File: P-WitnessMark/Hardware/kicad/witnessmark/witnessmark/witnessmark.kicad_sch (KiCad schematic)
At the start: 46 parts, among them J2 Conn_01x04, J3 Conn_01x11, J4 Conn_01x05, J5 USB_C_Receptacle_USB2.0_16P, U1 STM32U585RITx, U2 AP2112K-3.3, U3 SLS32AIA010MHUSON10XTMA2, U4 USBLC6-2SC6, Y1 Crystal

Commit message: WitnessMark: fix VDDA cap shorting GND to +3V3 (rail merge); GND now distinct
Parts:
- removed C8: 100nF, Capacitor_SMD:C_0603_1608Metric, symbol Device:C
- removed C9: 4.7µF, Capacitor_SMD:C_0603_1608Metric, symbol Device:C
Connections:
- net +3V3: no longer C1.2, C10.2, C11.2, C12.2, C13.1, C14.2, C15.2, C2.2, C3.2, C4.1, C5.1, C6.1, C7.1, J2.4 (Pin_4), J3.3 (Pin_3), J4.3 (Pin_3), J5.A1 (GND), J5.A12 (GND), J5.B1 (GND), J5.B12 (GND), J5.SH (SHIELD), R1.2, R4.1, R5.1, R6.2, S1.1, S1.2, U1.12 (VSSA), U1.18 (VSS), U1.31 (VSS), U1.47 (VSS), U1.63 (VSS), U2.2 (GND), U3.1 (GND), U3.11 (EP), U4.2 (GND)
- new net GND: C1.2, C10.2, C11.2, C12.2, C13.1, C14.2, C15.2, C2.2, C3.2, C4.1, C5.1, C6.1, C7.1, J2.4 (Pin_4), J3.3 (Pin_3), J4.3 (Pin_3), J5.A1 (GND), J5.A12 (GND), J5.B1 (GND), J5.B12 (GND), J5.SH (SHIELD), R1.2, R4.1, R5.1, R6.2, S1.1, S1.2, U1.12 (VSSA), U1.18 (VSS), U1.31 (VSS), U1.47 (VSS), U1.63 (VSS), U2.2 (GND), U3.1 (GND), U3.11 (EP), U4.2 (GND)
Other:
- moved on the sheet: J5, R4, R5

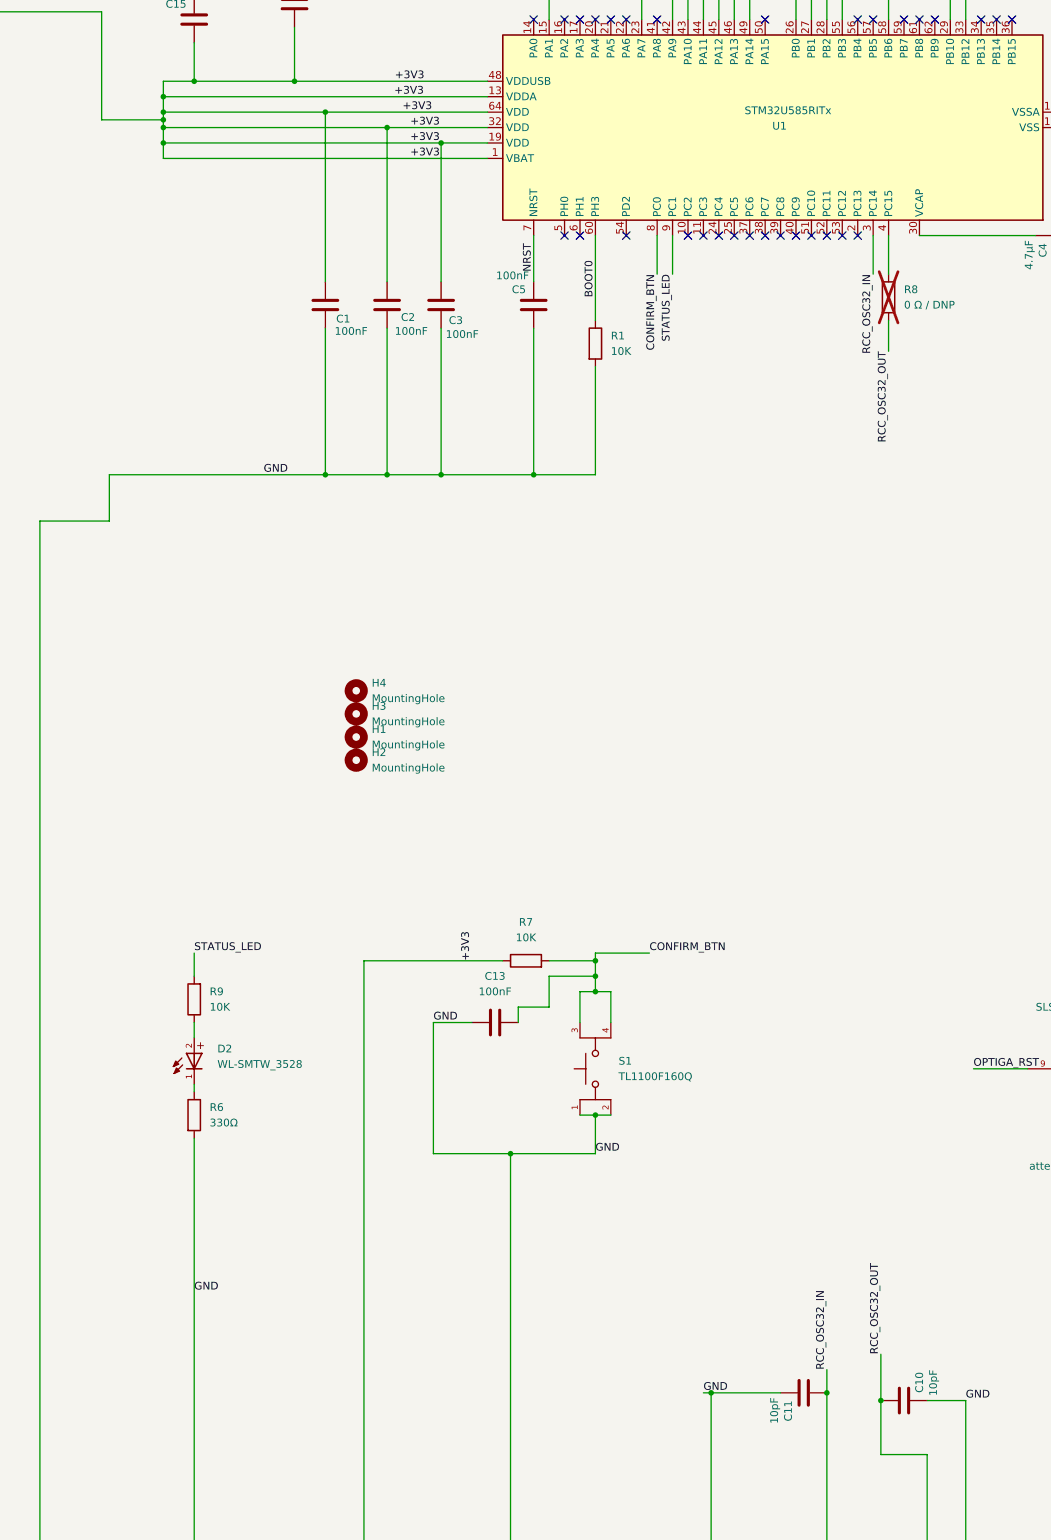
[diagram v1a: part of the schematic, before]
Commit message: Restore VDDA decoupling (C8/C9), crystal caps to 18pF, assign J5 footprint
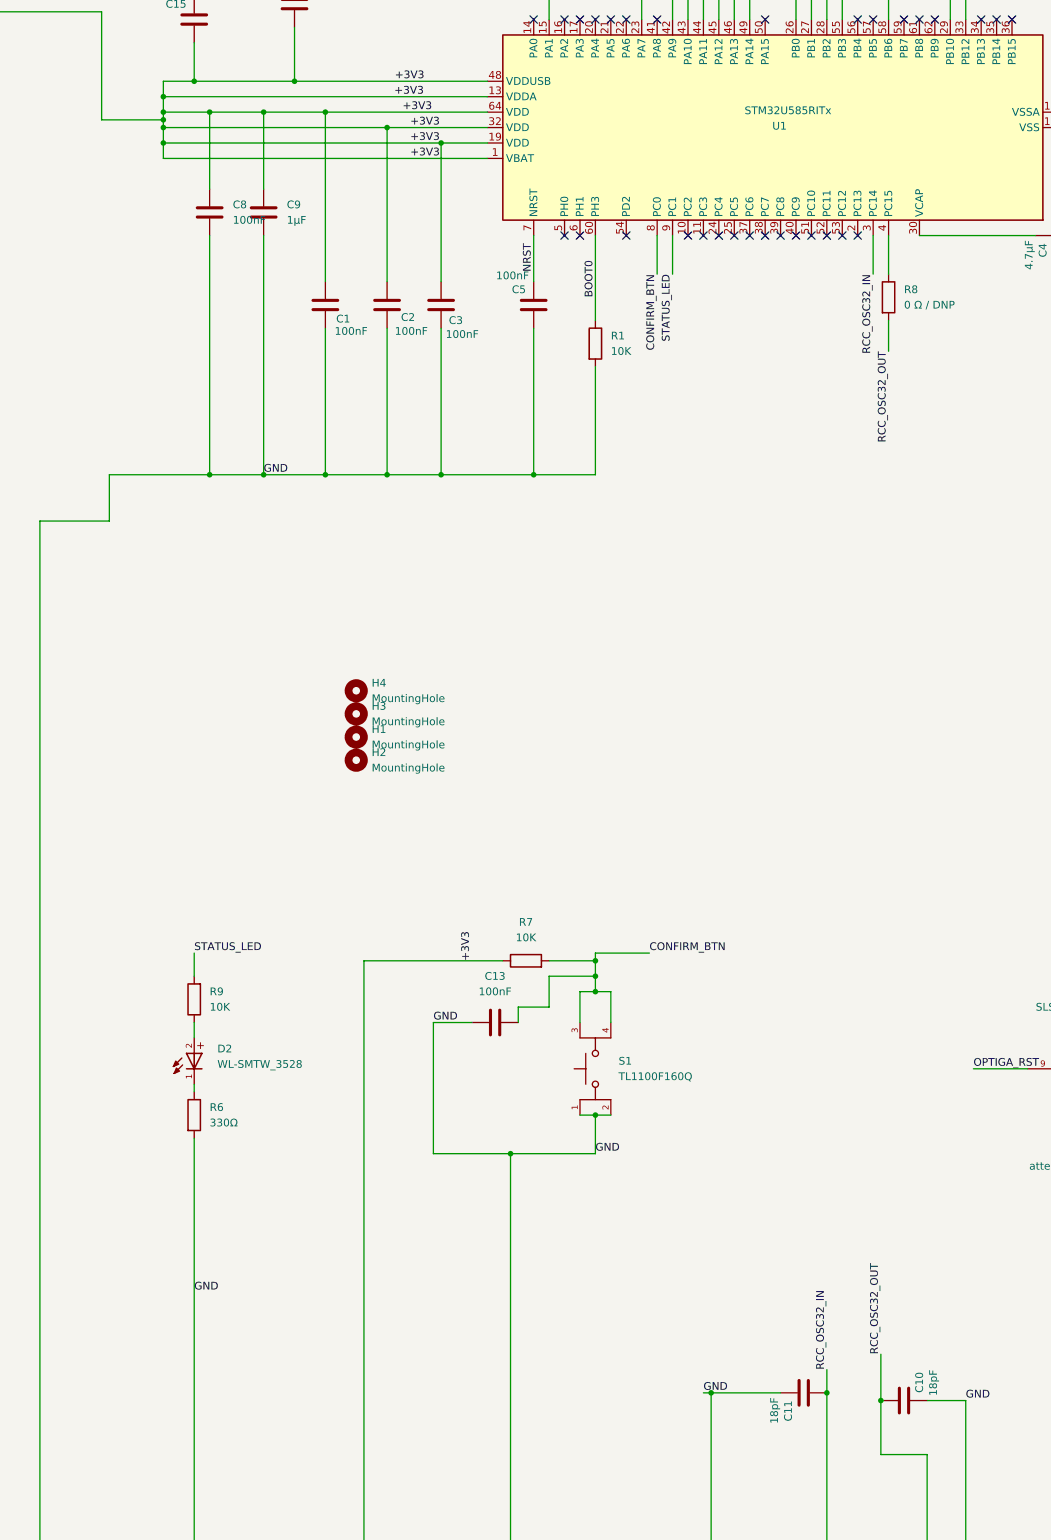
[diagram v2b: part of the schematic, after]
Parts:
- added C8: 100nF, Capacitor_SMD:C_0603_1608Metric, symbol Device:C
- added C9: 1µF, Capacitor_SMD:C_0603_1608Metric, symbol Device:C
- C10, C11: value 10pF -> 18pF
- J5: footprint (none) -> Connector_USB:USB_C_Receptacle_GCT_USB4105-xx-A_16P_TopMnt_Horizontal
- R8: now fitted
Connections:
- net +3V3: now also C8.2, C9.2
- net GND: now also C8.1, C9.1

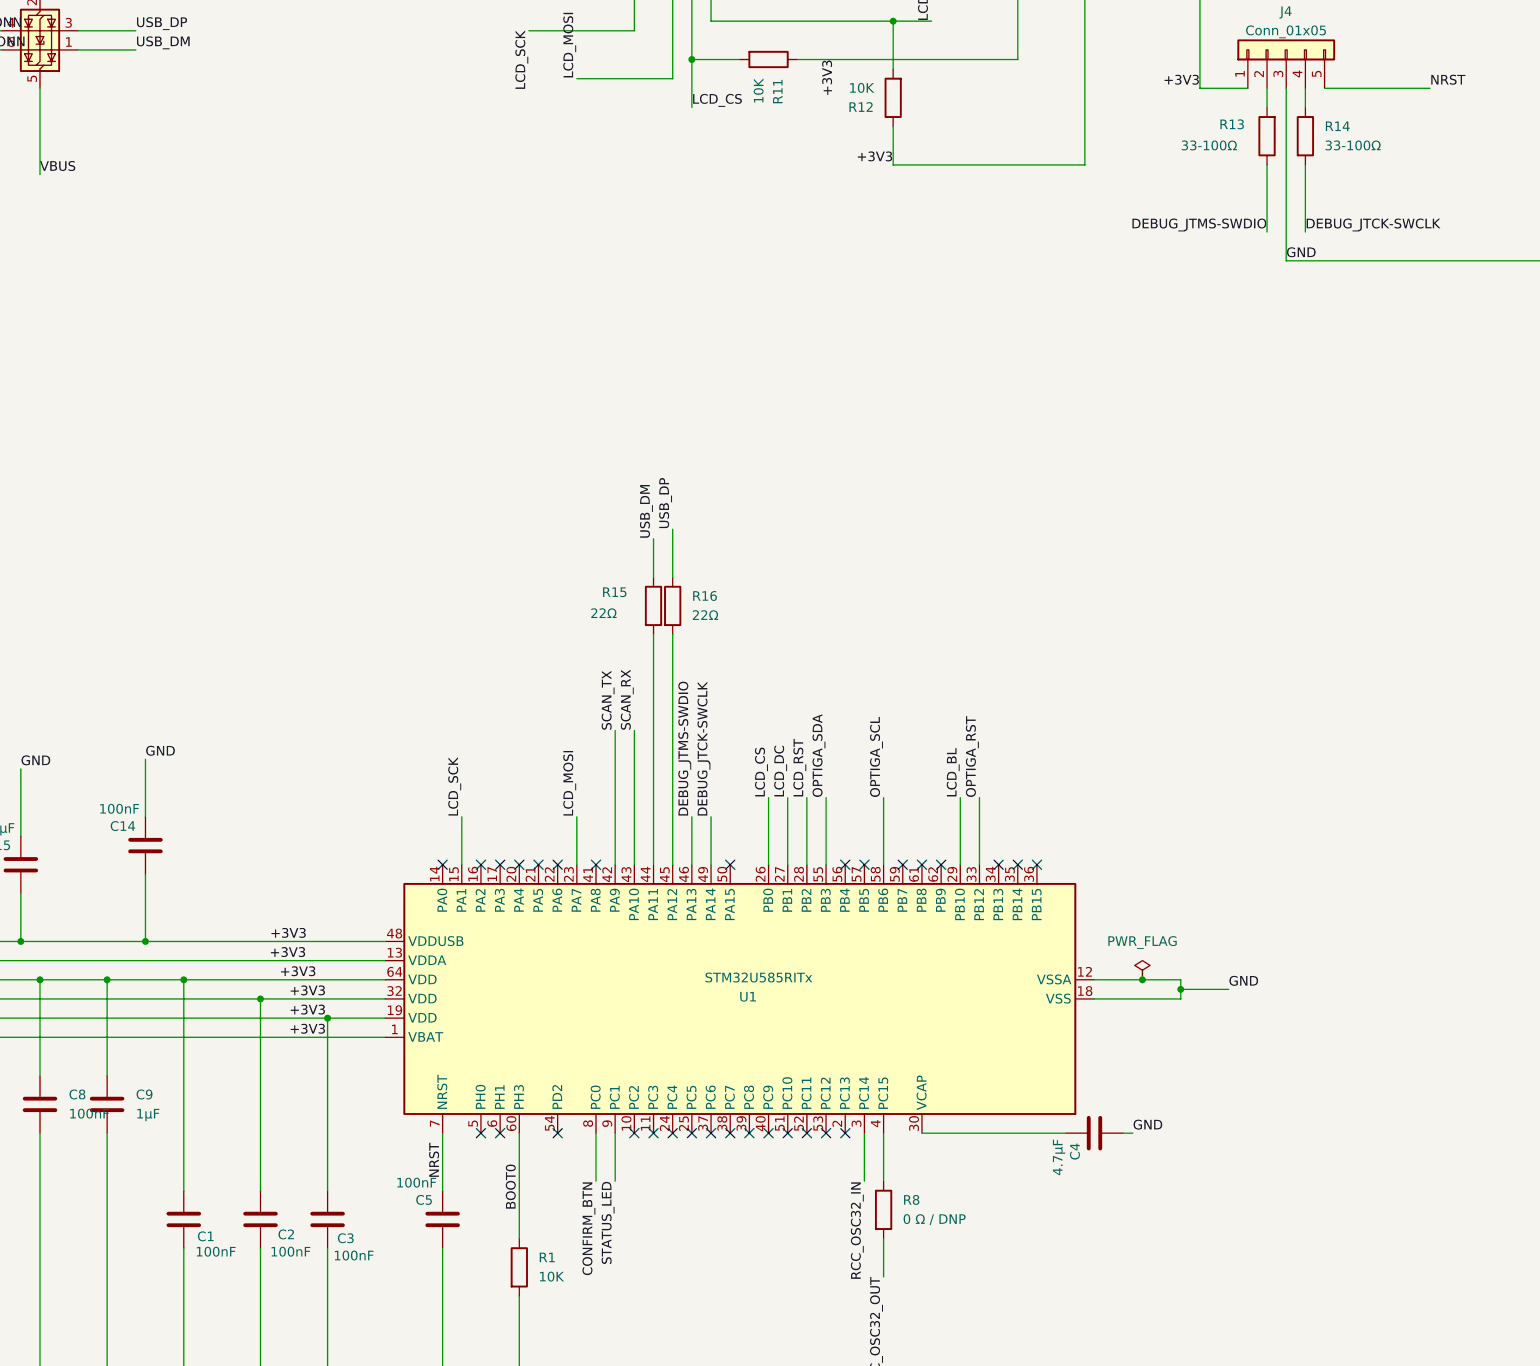
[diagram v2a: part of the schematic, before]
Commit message: WitnessMark schematic: BOOT0/J3 grounds, USB Rs 0R, SWD direct
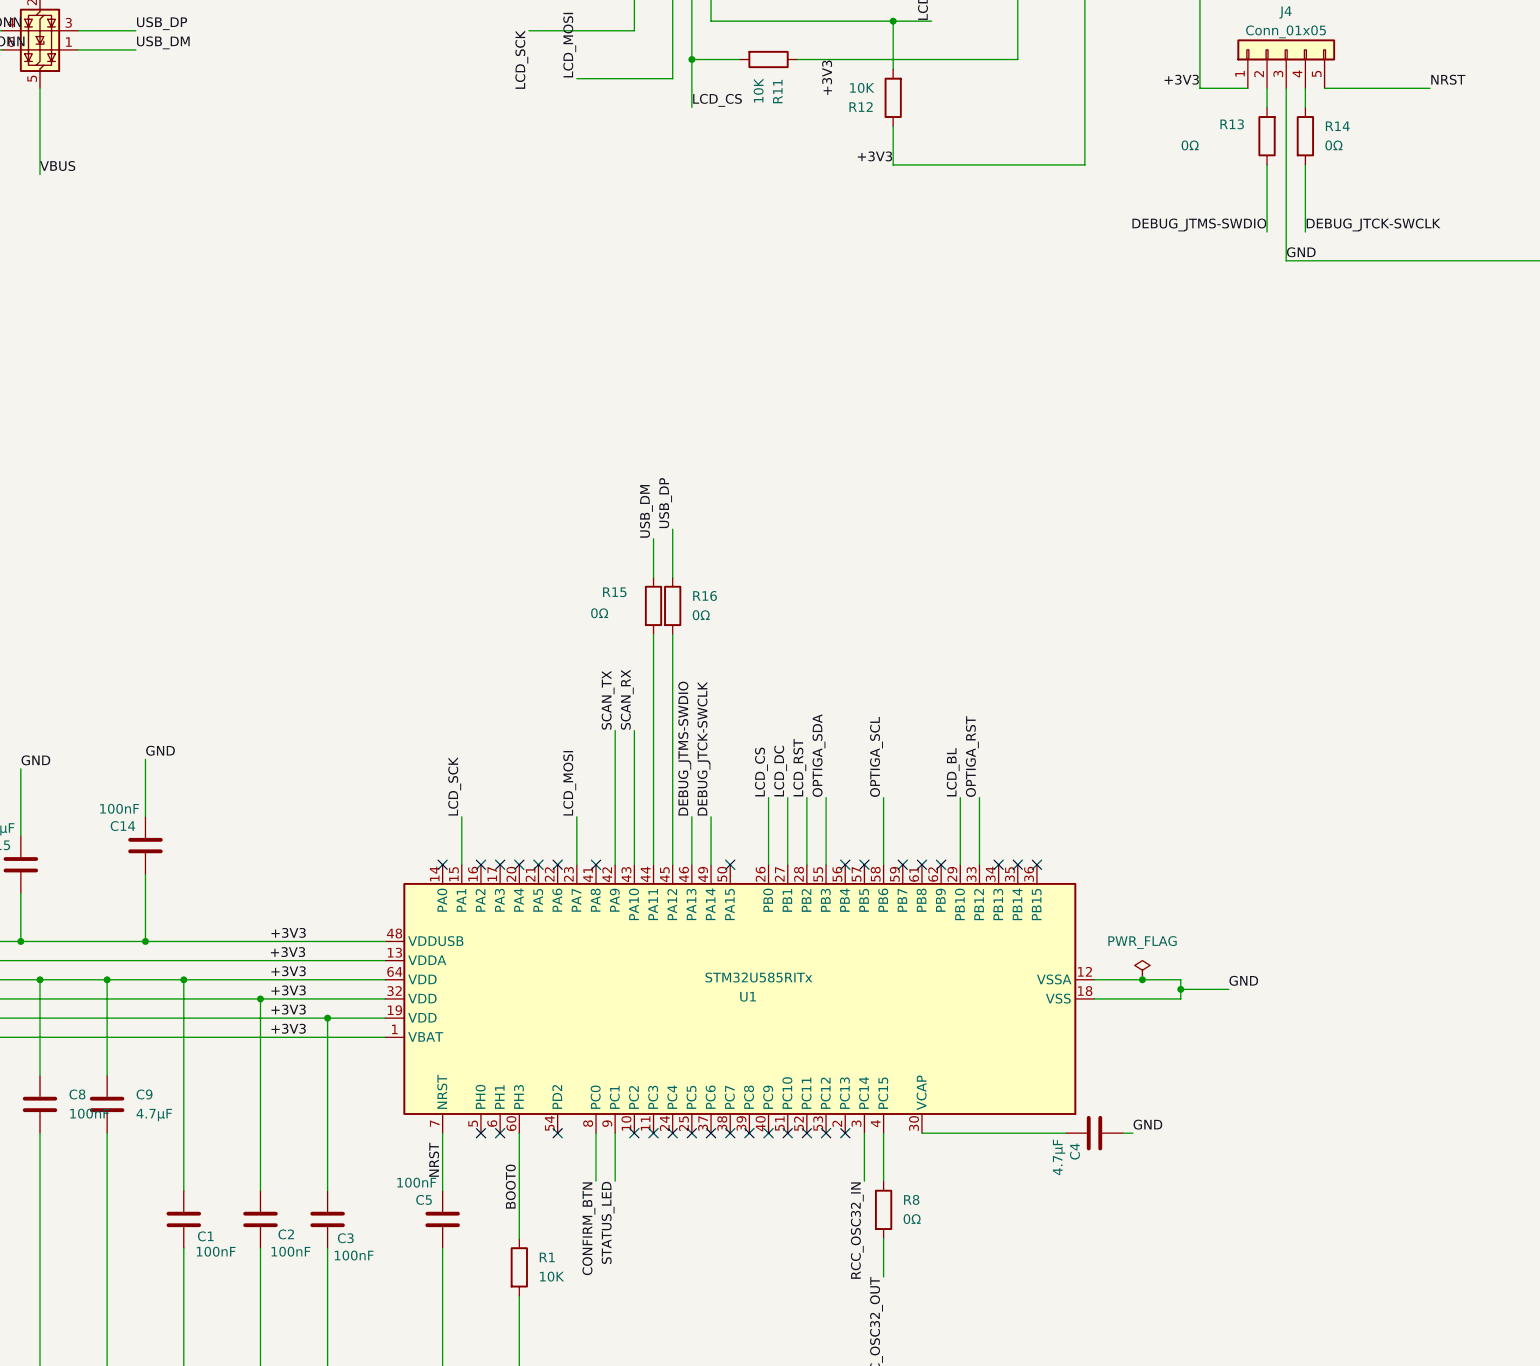
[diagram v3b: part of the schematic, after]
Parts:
- C9: value 1µF -> 4.7µF
- R13, R14: value 33-100Ω -> 0Ω
- R15, R16: value 22Ω -> 0Ω
- R8: value 0 Ω / DNP -> 0Ω
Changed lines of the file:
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@@
 	)
 	(label "+3V3"
-		(at 105.41 90.17 0)
+		(at 102.87 90.17 0)
 		(effects
 			(font
@@
 	)
 	(label "+3V3"
-		(at 105.41 92.71 0)
+		(at 102.87 92.71 0)
 		(effects
 			(font
@@
 	)
 	(label "+3V3"
-		(at 105.41 87.63 0)
+		(at 102.87 87.63 0)
 		(effects
 			(font
@@
 	)
 	(label "+3V3"
-		(at 104.1399 85.09 0)
+		(at 102.87 85.09 0)
 		(effects
 			(font
@@
 			)
 		)
-		(property "Value" "22Ω"
+		(property "Value" "0Ω"
 			(at 158.75 36.8299 0)
 			(show_name no)
@@
 			)
 		)
-		(property "Value" "1µF"
+		(property "Value" "4.7µF"
 			(at 85.09 102.8699 0)
 			(show_name no)
@@
 			)
 		)
-		(property "Value" "33-100Ω"
+		(property "Value" "0Ω"
 			(at 223.52 -25.4 0)
 			(show_name no)
@@
 			)
 		)
-		(property "Value" "0 Ω / DNP"
+		(property "Value" "0Ω"
 			(at 186.69 116.8399 0)
 			(show_name no)
@@
 			)
 		)
-		(property "Value" "22Ω"
+		(property "Value" "0Ω"
 			(at 145.288 36.576 0)
 			(show_name no)
@@
 			)
 		)
-		(property "Value" "33-100Ω"
+		(property "Value" "0Ω"
 			(at 242.57 -25.4001 0)
 			(show_name no)

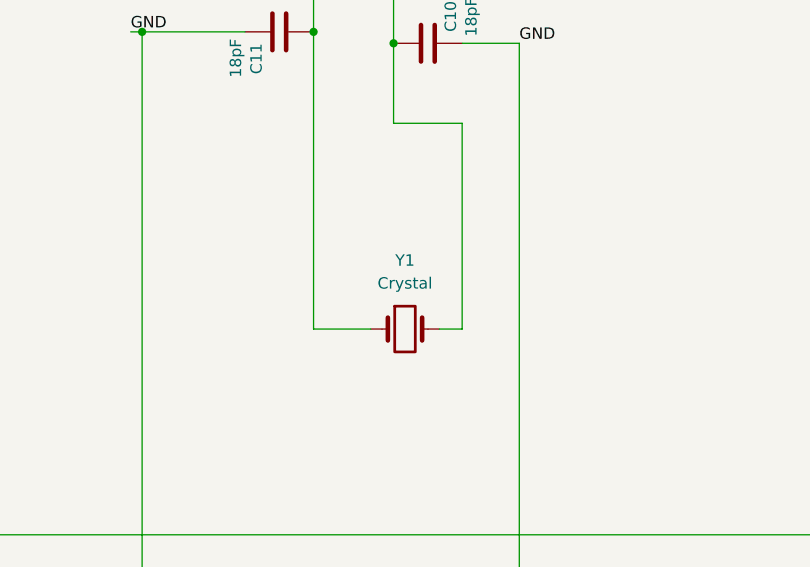
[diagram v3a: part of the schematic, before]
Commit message: WitnessMark schematic: BOOT0/J3 grounds, all caps grounded, USB Rs 0R, SWD direct, crystal 18pF
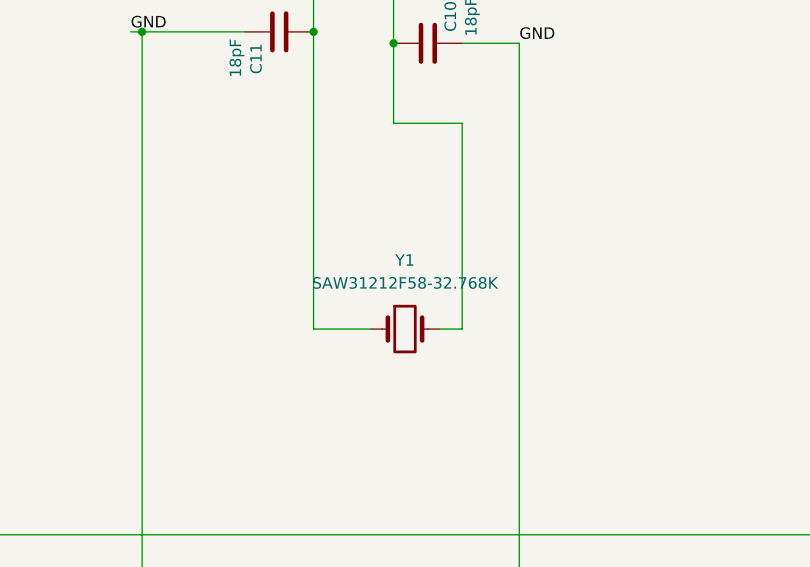
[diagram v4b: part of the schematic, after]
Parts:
- Y1: value Crystal -> SAW31212F58-32.768K
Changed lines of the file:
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@@
 			)
 		)
-		(property "Value" "Crystal"
+		(property "Value" "SAW31212F58-32.768K"
 			(at 184.15 323.85 0)
 			(show_name no)
